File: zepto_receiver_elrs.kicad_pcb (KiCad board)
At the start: 4 copper layers, 9.5 x 7.5 mm, 38 parts, among them J1 u.fl, U1 STM32WLE5JBI6, U2 NCP160, U3 BGS12PL6E6327XTSA1, U4 0900FM15D0039, U5 ECS-TXO-25CSMV-320-AM-TR

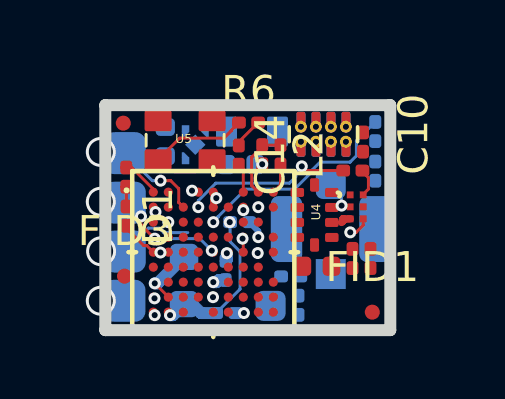
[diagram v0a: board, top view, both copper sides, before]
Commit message: connect SWDIO in layout
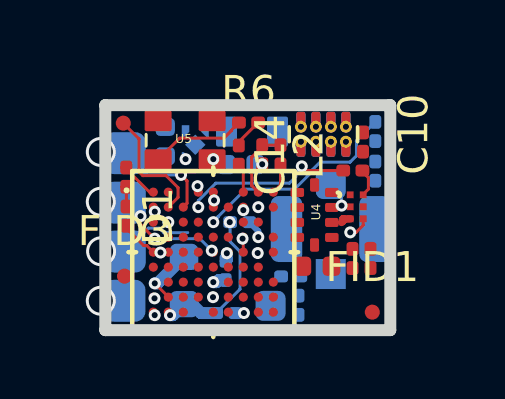
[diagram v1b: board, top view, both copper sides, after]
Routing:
- net SWDIO: track 0.00 -> 4.14 mm
- net +3V3: track 3.77 -> 3.70 mm, vias 8 -> 9
- net GND: track 3.79 -> 3.77 mm, vias 11 -> 12
